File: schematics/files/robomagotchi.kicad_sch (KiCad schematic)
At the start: 23 parts, among them M1 Servo Motor, U1 SPI LCD Display (ST7735), U2 I2C OLED Display (GM009605), U3 Ultrasonic Proximity Sensor (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, U4 Temp Sensor (DHT11), U5 IR Receiver (VS18838B)

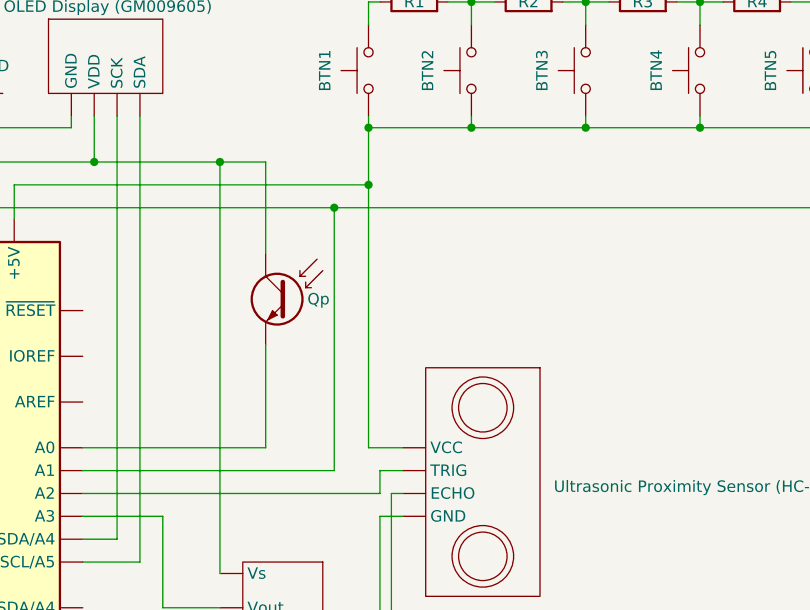
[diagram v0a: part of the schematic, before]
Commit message: Fixed schematic error
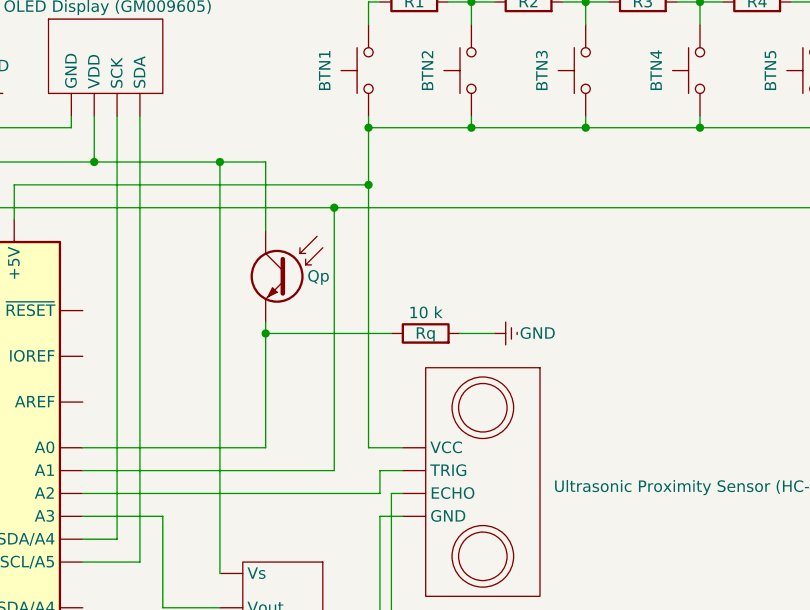
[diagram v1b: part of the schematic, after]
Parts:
- added Rq: 10 k, symbol Device:R
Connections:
- net GND: now also Rq.2
- net at A2.9 (A0), Qp.2 (E): now also Rq.1
- new net: A2.4 (3V3), Qp.1 (C), U1. (VCC), U2. (VDD), U4. (Vs), U5. (VCC)
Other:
- moved on the sheet: Qp
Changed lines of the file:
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@@
 	(title_block
 		(title "Robomagotchi Electronic Circuit")
-		(date "2024-12-16")
-		(rev "1.1")
+		(date "2024-12-17")
+		(rev "1.2")
 		(company "Author: Adrian-Mihael Fota")
 		(comment 1 "University of Bucharest")
@@
 	)
 	(junction
+		(at 163.83 93.98)
+		(diameter 0)
+		(color 0 0 0 0)
+	)
+	(junction
 		(at 212.09 57.15)
 		(diameter 0)
@@
 	(wire
 		(pts
+			(xy 163.83 93.98) (xy 177.8 93.98)
+		)
+		(stroke
+			(width 0)
+			(type default)
+		)
+	)
+	(wire
+		(pts
 			(xy 142.24 69.85) (xy 142.24 71.12)
 		)
@@
 	(wire
 		(pts
+			(xy 163.83 93.98) (xy 163.83 92.71)
+		)
+		(stroke
+			(width 0)
+			(type default)
+		)
+	)
+	(wire
+		(pts
 			(xy 114.3 140.97) (xy 114.3 147.32)
 		)
@@
 	(wire
 		(pts
-			(xy 163.83 85.09) (xy 163.83 74.93)
+			(xy 163.83 82.55) (xy 163.83 74.93)
 		)
 		(stroke
@@
 	(wire
 		(pts
-			(xy 163.83 106.68) (xy 163.83 95.25)
+			(xy 163.83 106.68) (xy 163.83 93.98)
 		)
 		(stroke
@@
 	(wire
 		(pts
+			(xy 185.42 93.98) (xy 189.23 93.98)
+		)
+		(stroke
+			(width 0)
+			(type default)
+		)
+	)
+	(wire
+		(pts
 			(xy 118.11 119.38) (xy 101.6 119.38)
 		)
@@
 	(symbol
 		(lib_id "Sensor_Optical:SFH309")
-		(at 166.37 90.17 0)
+		(at 166.37 87.63 0)
 		(mirror y)
 		(unit 1)
@@
 		(dnp no)
 		(property "Reference" "Qp"
-			(at 170.942 90.17 0)
+			(at 170.942 87.63 0)
 			(effects
 				(font
@@
 		)
 		(property "Value" "Phototransistor"
-			(at 161.29 90.6906 0)
+			(at 161.29 88.1506 0)
 			(effects
 				(font
@@
 		)
 		(property "Footprint" "LED_THT:LED_D3.0mm_Clear"
-			(at 154.178 93.726 0)
+			(at 154.178 91.186 0)
 			(effects
 				(font
@@
 		)
 		(property "Datasheet" "http://www.osram-os.com/Graphics/XPic2/00101811_0.pdf/SFH%20309,%20SFH%20309%20FA,%20Lead%20(Pb)%20Free%20Product%20-%20RoHS%20Compliant.pdf"
-			(at 166.37 90.17 0)
+			(at 166.37 87.63 0)
 			(effects
 				(font
@@
 		)
 		(property "Description" "Phototransistor NPN"
-			(at 166.37 90.17 0)
+			(at 166.37 87.63 0)
 			(effects
 				(font
@@
 					(unit 1)
 				)
+			)
+		)
+	)
+	(symbol
+		(lib_id "Device:R")
+		(at 181.61 93.98 90)
+		(unit 1)
+		(exclude_from_sim no)
+		(in_bom yes)
+		(on_board yes)
+		(dnp no)
+		(property "Reference" "Rq"
+			(at 181.61 93.98 90)
+			(effects
+				(font
+					(size 1.27 1.27)
+				)
+			)
+		)
+		(property "Value" "10 k"
+			(at 181.61 91.694 90)
+			(effects
+				(font
+					(size 1.27 1.27)
+				)
+			)
+		)
+		(property "Footprint" ""
+			(at 181.61 95.758 90)
+			(effects
+				(font
+					(size 1.27 1.27)
+				)
+				(hide yes)
+			)
+		)
+		(property "Datasheet" "~"
+			(at 181.61 93.98 0)
+			(effects
+				(font
+					(size 1.27 1.27)
+				)
+				(hide yes)
+			)
+		)
+		(property "Description" "Resistor"
+			(at 181.61 93.98 0)
+			(effects
+				(font
+					(size 1.27 1.27)
+				)
+				(hide yes)
+			)
+		)
+		(pin "1"
+		)
+		(pin "2"
+		)
+		(instances
+			(project "robomagotchi"
+				(path "/564f43e2-925d-4726-ad2e-2e1f480b3347"
+					(reference "Rq")
+					(unit 1)
+				)
+			)
+		)
+	)
+	(symbol
+		(lib_id "power:Earth")
+		(at 189.23 93.98 90)
+		(unit 1)
+		(exclude_from_sim no)
+		(in_bom yes)
+		(on_board yes)
+		(dnp no)
+		(property "Reference" "#PWR06"
+			(at 195.58 93.98 0)
+			(effects
+				(font
+					(size 1.27 1.27)
+				)
+				(hide yes)
+			)
+		)
+		(property "Value" "GND"
+			(at 194.056 93.98 90)
+			(effects
+				(font
+					(size 1.27 1.27)
+				)
+			)
+		)
+		(property "Footprint" ""
+			(at 189.23 93.98 0)
+			(effects
+				(font
+					(size 1.27 1.27)
+				)
+				(hide yes)
+			)
+		)
+		(property "Datasheet" "~"
+			(at 189.23 93.98 0)
+			(effects
+				(font
+					(size 1.27 1.27)
+				)
+				(hide yes)
+			)
+		)
+		(property "Description" "Power symbol creates a global label with name \"Earth\""
+			(at 189.23 93.98 0)
+			(effects
+				(font
+					(size 1.27 1.27)
+				)
+				(hide yes)
+			)
+		)
+		(pin "1"
+		)
+		(instances
+			(project "robomagotchi"
+				(path "/564f43e2-925d-4726-ad2e-2e1f480b3347"
+					(reference "#PWR06")
+					(unit 1)
+				)

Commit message: Updated Schematic
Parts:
- R1: value 220 Ω -> 1 k
- R3: value 2 k -> 1 k
- R4: value 5.1 k -> 2 k
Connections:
- new net: A2.4 (3V3), Qp.1 (C), U1. (VCC), U2. (VDD), U4. (Vs), U5. (VCC)
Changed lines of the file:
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@@
 		(title "Robomagotchi Electronic Circuit")
 		(date "2024-12-17")
-		(rev "1.2")
+		(rev "1.3")
 		(company "Author: Adrian-Mihael Fota")
 		(comment 1 "University of Bucharest")
@@
 			)
 		)
-		(property "Value" "220 Ω"
+		(property "Value" "1 k"
 			(at 180.34 54.864 90)
 			(effects
@@
 			)
 		)
-		(property "Value" "2 k"
+		(property "Value" "1 k"
 			(at 205.74 54.864 90)
 			(effects
@@
 			)
 		)
-		(property "Value" "5.1 k"
+		(property "Value" "2 k"
 			(at 218.44 54.864 90)
 			(effects

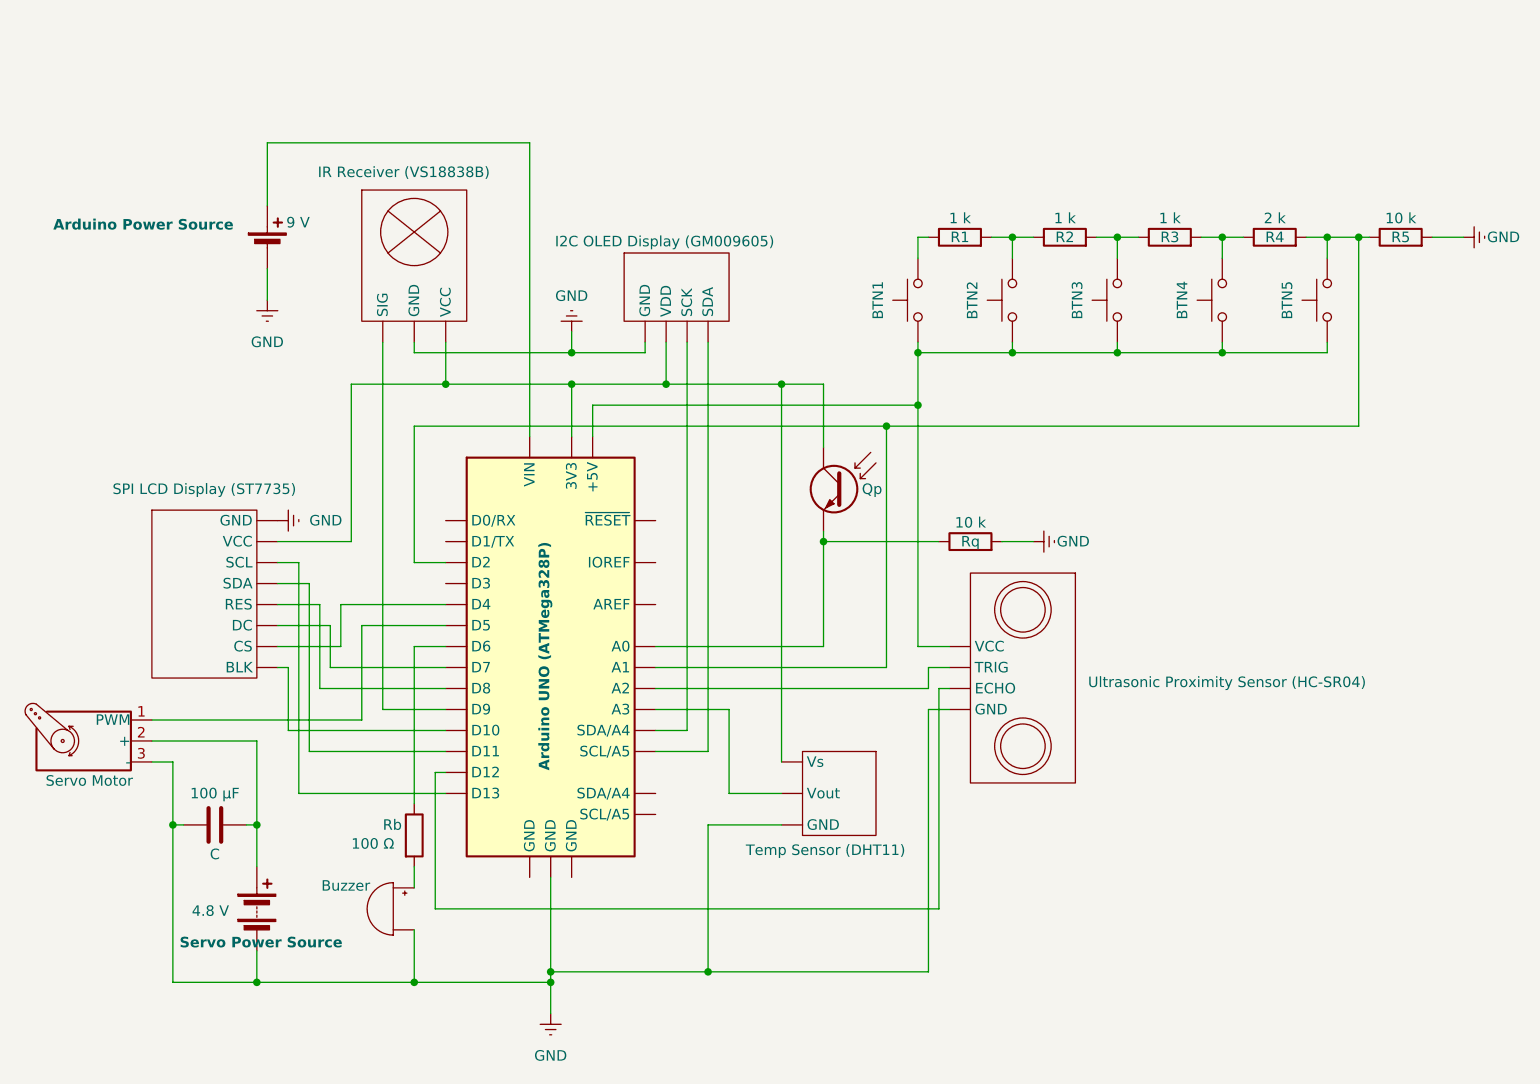
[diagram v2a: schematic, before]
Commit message: Replaced 4.8V power source with voltage divider
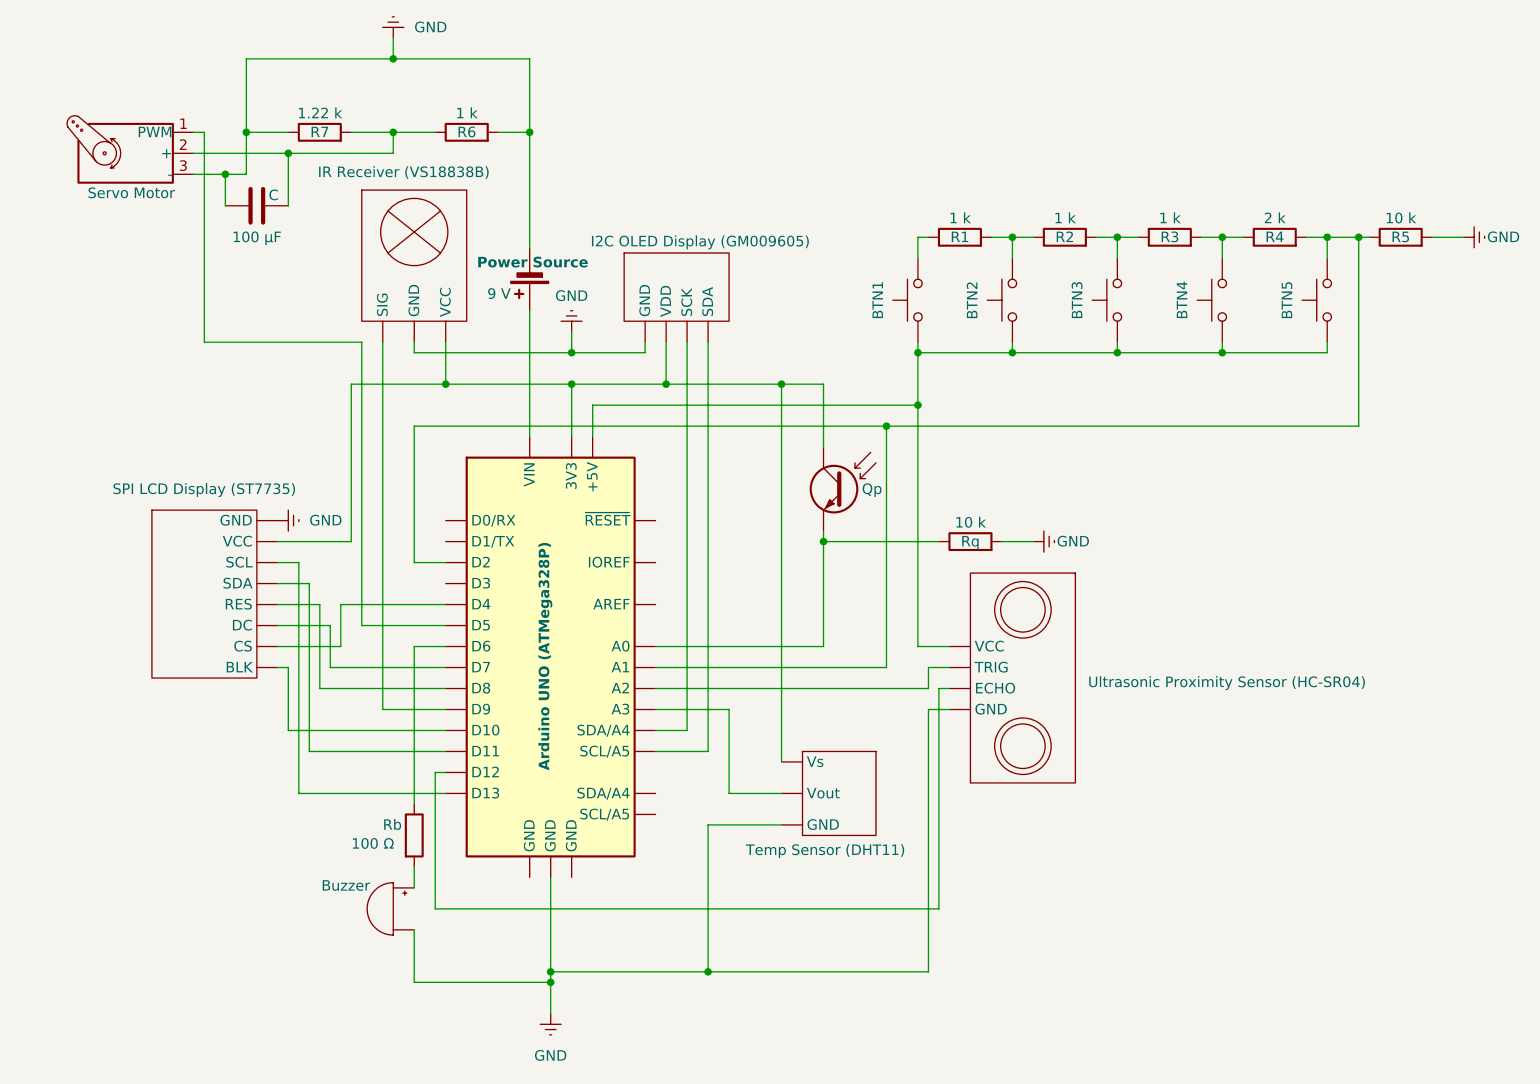
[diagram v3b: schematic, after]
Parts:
- removed BT1: 4.8 V, symbol Device:Battery
- added R6: 1 k, symbol Device:R
- added R7: 1.22 k, symbol Device:R
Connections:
- net GND: now also R6.2, R7.1
- net at C.2, M1.2 (+): now also R6.1, R7.2
- new net: A2.4 (3V3), Qp.1 (C), U1. (VCC), U2. (VDD), U4. (Vs), U5. (VCC)
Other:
- moved on the sheet: C

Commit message: Fixed an error in the schematic
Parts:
- added R8: 220 Ω, symbol Device:R
- R7: value 1.22 k -> 1 k
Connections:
- net GND: now also R8.1; no longer R6.2, R7.1
- net at A2.8 (VIN), BT2.1 (+): now also R6.2
- new net: A2.4 (3V3), Qp.1 (C), U1. (VCC), U2. (VDD), U4. (Vs), U5. (VCC)
- new net: R7.1, R8.2
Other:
- moved on the sheet: R7

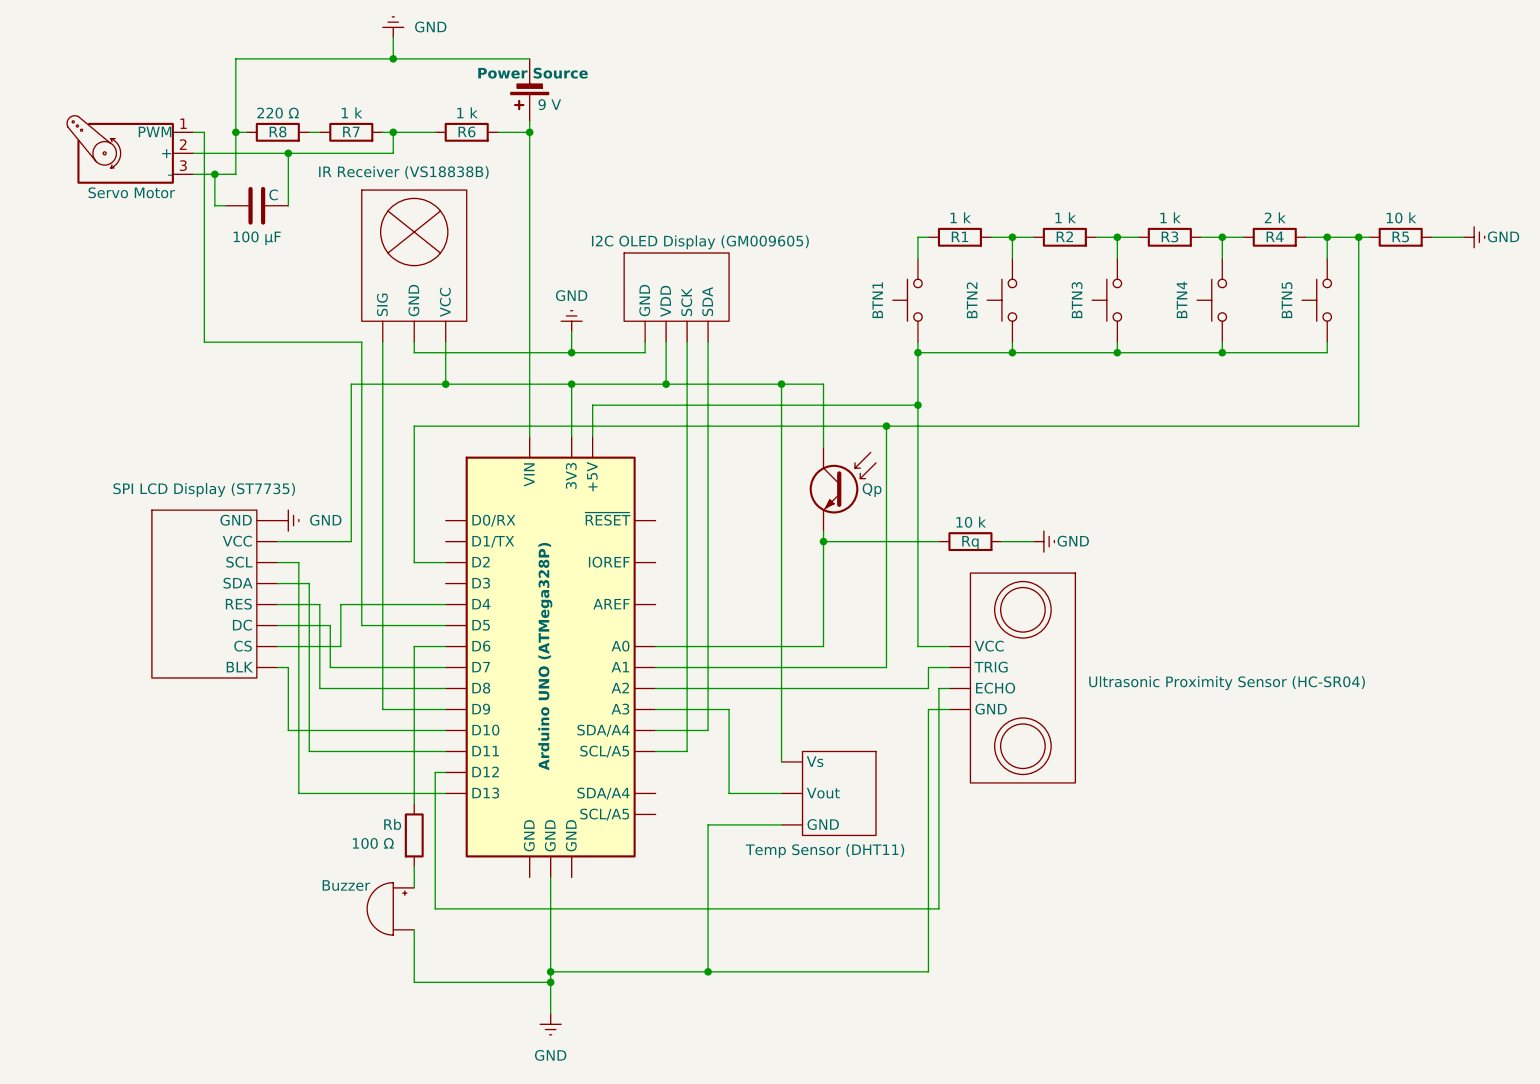
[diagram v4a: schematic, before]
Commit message: Replaced ST7735 with ILI9341
Also fixed error in DHT11 pins and updated schematic accordingly.
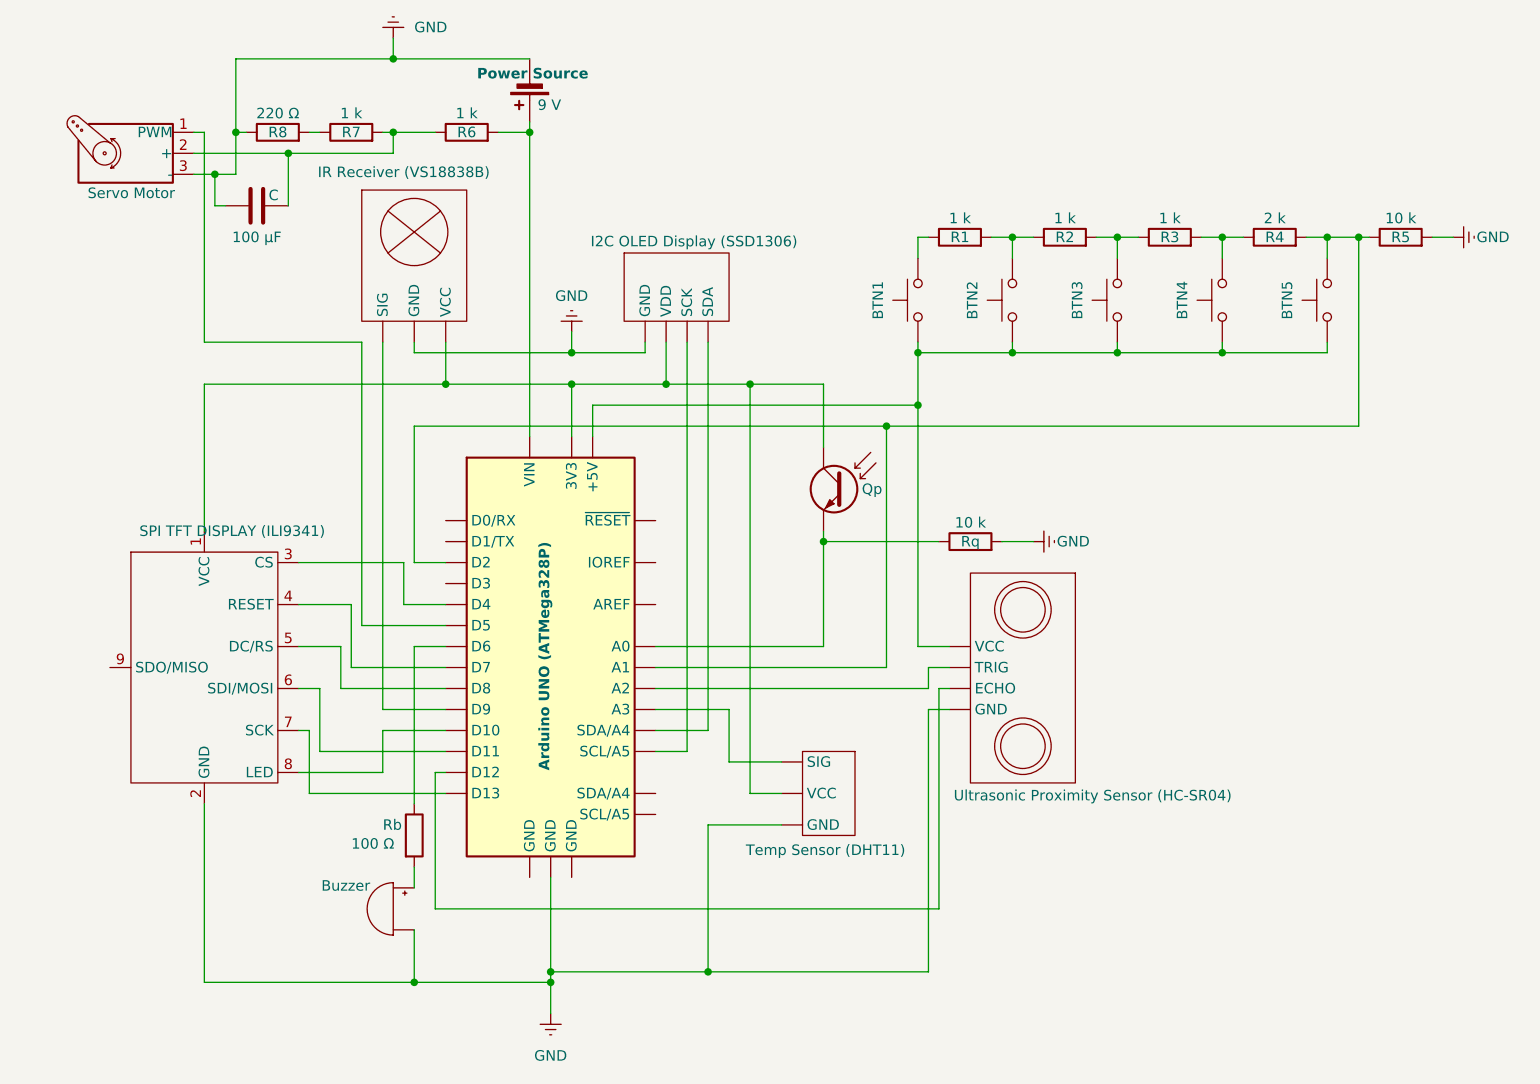
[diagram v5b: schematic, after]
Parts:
- removed U1: SPI LCD Display (ST7735), symbol My_Symbols:DISPLAY_128_ST7735S
- added U1: SPI TFT DISPLAY (ILI9341), symbol A_LAPTOP_LIB:ILI9341_SPI_TFT
- U2: value I2C OLED Display (GM009605) -> I2C OLED Display (SSD1306)
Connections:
- net GND: now also U1.2 (GND)
- net at A2.19 (D4): now also U1.3 (CS)
- net at A2.22 (D7): now also U1.4 (RESET)
- net at A2.23 (D8): now also U1.5 (DC/RS)
- net at A2.25 (D10): now also U1.8 (LED)
- net at A2.26 (D11): now also U1.6 (SDI/MOSI)
- net at A2.28 (D13): now also U1.7 (SCK)
- new net: A2.4 (3V3), Qp.1 (C), U1.1 (VCC), U2. (VDD), U4. (VCC), U5. (VCC)
